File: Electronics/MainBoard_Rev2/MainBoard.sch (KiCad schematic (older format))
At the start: 4 parts

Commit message: Rev 3.0 is now done!
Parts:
- added D6: LED_Dual_AACC, LED_SMD:LED_RGB_1210, symbol Device:LED_Dual_AACC
- added D7: LED, LED_SMD:LED_0603_1608Metric, symbol Device:LED
- added H1, H2: MountingHole, MountingHole:MountingHole_3.2mm_M3_DIN965, symbol Mechanical:MountingHole
- added H3: MountingHole, Symbol:KiCad-Logo_5mm_SolderMask, symbol Mechanical:MountingHole
- added H4: MountingHole, Symbol:OSHW-Logo_5.7x6mm_SilkScreen, symbol Mechanical:MountingHole
- added H5: MountingHole, MainBoard_Rev2:QR_Link, symbol Mechanical:MountingHole
- added H6: MountingHole, MainBoard_Rev2:DragonIcon, symbol Mechanical:MountingHole
- added J1: Conn_01x04_Female, Connector_PinSocket_2.54mm:PinSocket_1x04_P2.54mm_Vertical, symbol Connector:Conn_01x04_Female
- added R2, R3, R5, R6: 2.2k, Resistor_SMD:R_0603_1608Metric, symbol Device:R_Small
- added R4: 220, Resistor_SMD:R_0603_1608Metric, symbol Device:R_Small
- C1, C2: renamed from C?; footprint (none) -> Capacitor_SMD:C_0603_1608Metric
- J2: renamed from J?; footprint (none) -> Connector_Dsub:DSUB-9_Female_Horizontal_P2.77x2.84mm_EdgePinOffset4.94mm_Housed_MountingHolesOffset7.48mm; Digi-Key (none) -> AE10921-ND; MPN (none) -> A-DF 09 A/KG-T2S
- U1: renamed from U?; Digi-Key (none) -> 1904-1025-1-ND; MPN (none) -> ESP32-WROOM-32D (16MB)
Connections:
- net +3V3: now also D6.1 (A1), D6.2 (A2), D7.2 (A), J1.2 (Pin_2), R5.1, R6.1
- net GND: now also J1.1 (Pin_1)
- net AUDIO: now reaches U1.10 (IO25)
- net IR_OUT: now reaches U1.11 (IO26)
- net LED_1: now reaches U1.12 (IO27)
- net VBRT: now reaches U1.16 (IO13)
- net TRIGGER: now reaches U1.23 (IO15)
- net IR_IN: now reaches U1.24 (IO2)
- net IR_IN: now also J2.3
- net CHG_STAT: now reaches U1.26 (IO4)
- net SDA: now reaches U1.27 (IO16)
- net SDA: now also J2.8, J1.4 (Pin_4), R6.2
- net SCL: now reaches U1.28 (IO17)
- net SCL: now also J2.4, J1.3 (Pin_3), R5.2
- net CHG_R: now reaches U1.30 (IO18)
- net CHG_R: now also R2.2
- net CHG_G: now reaches U1.31 (IO19)
- net CHG_G: now also R3.2
- net CONN_IND: now reaches U1.33 (IO21)
- net CONN_IND: now also R4.2
- net V_SENSE: now reaches U1.9 (IO33)
- net LED_2: now reaches J2.7
- new net: D6.4 (K2), R2.1
- new net: D6.3 (K1), R3.1
- new net: D7.1 (K), R4.1
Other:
- moved on the sheet: J2

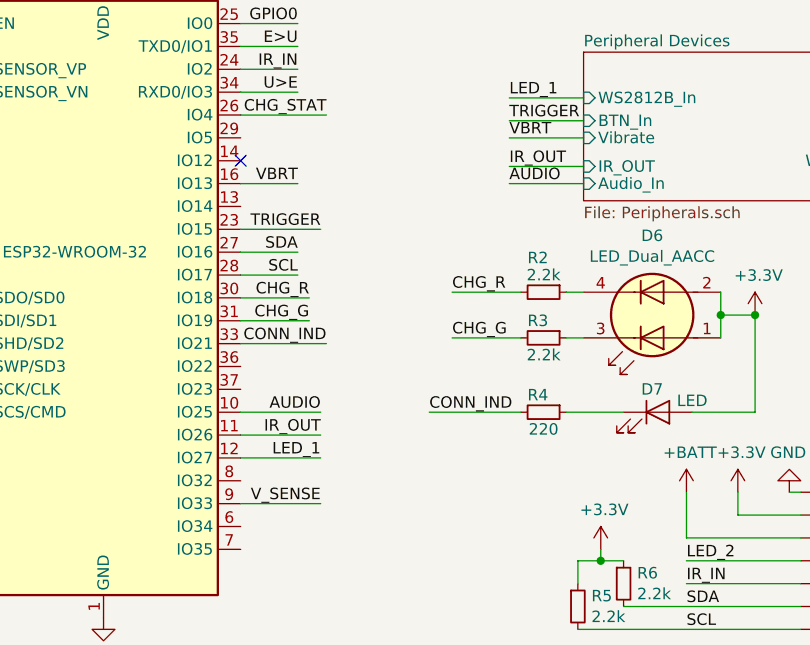
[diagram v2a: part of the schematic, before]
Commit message: Adjusted a few resistor values, added I2S pinout
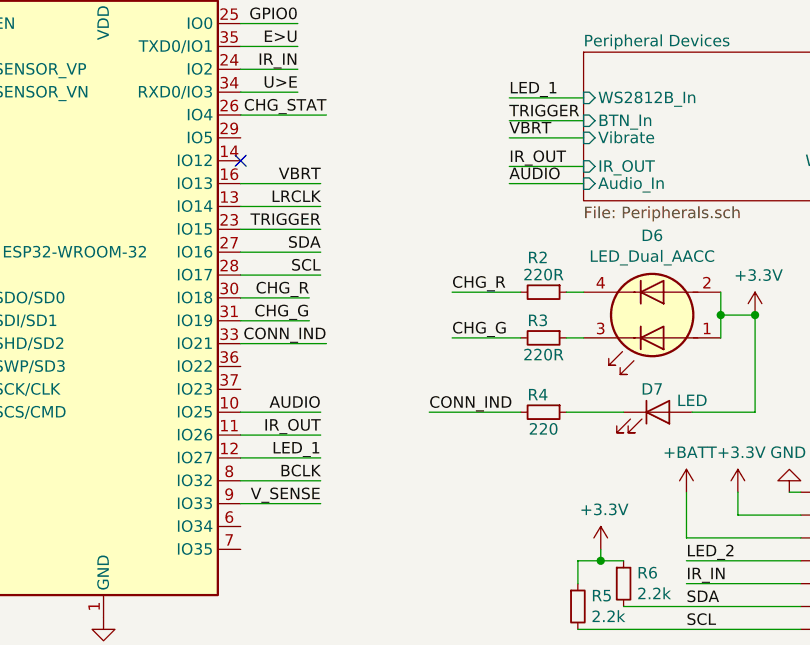
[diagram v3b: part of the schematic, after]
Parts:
- R2, R3: value 2.2k -> 220R
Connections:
- net LRCLK: now reaches U1.13 (IO14)
- net BCLK: now reaches U1.8 (IO32)
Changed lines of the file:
@@
 	6900 4400 6550 4400
 Wire Wire Line
-	6550 3000 6800 3000
-Text Label 6800 3000 2    50   ~ 0
+	6550 3000 6900 3000
+Text Label 6900 3000 2    50   ~ 0
 VBRT
 Text Label 7725 2800 0    50   ~ 0
@@
 P 7875 3475
 F 0 "R2" V 7725 3450 50  0000 C CNN
-F 1 "2.2k" V 7800 3475 50  0000 C CNN
+F 1 "220R" V 7800 3475 50  0000 C CNN
 F 2 "Resistor_SMD:R_0603_1608Metric" H 7875 3475 50  0001 C CNN
 F 3 "~" H 7875 3475 50  0001 C CNN
@@
 P 7875 3675
 F 0 "R3" V 7800 3650 50  0000 C CNN
-F 1 "2.2k" V 7950 3675 50  0000 C CNN
+F 1 "220R" V 7950 3675 50  0000 C CNN
 F 2 "Resistor_SMD:R_0603_1608Metric" H 7875 3675 50  0001 C CNN
 F 3 "~" H 7875 3675 50  0001 C CNN
@@
 IR_IN
 Wire Wire Line
-	6550 3300 6800 3300
-Wire Wire Line
-	6550 3400 6800 3400
-Text Label 6800 3300 2    50   ~ 0
+	6550 3300 6900 3300
+Wire Wire Line
+	6550 3400 6900 3400
+Text Label 6900 3300 2    50   ~ 0
 SDA
-Text Label 6800 3400 2    50   ~ 0
+Text Label 6900 3400 2    50   ~ 0
 SCL
 $Comp
@@
 Wire Wire Line
 	2600 3575 2600 4325
+Text Label 6900 4300 2    50   ~ 0
+BCLK
+Text Label 6900 3100 2    50   ~ 0
+LRCLK
+Wire Wire Line
+	6550 4300 6900 4300
+Wire Wire Line
+	6550 3100 6900 3100
 $EndSCHEMATC

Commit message: Began rework to even better hardware
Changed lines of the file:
@@
 Text Label 6800 2500 2    50   ~ 0
 IR_IN
-Wire Wire Line
-	6550 3300 6900 3300
-Wire Wire Line
-	6550 3400 6900 3400
 Text Label 6900 3300 2    50   ~ 0
 SDA
@@
 Wire Wire Line
 	6550 3100 6900 3100
+Text GLabel 6925 3300 2    50   Input ~ 0
+SDA
+Text GLabel 6925 3400 2    50   Input ~ 0
+SCL
+Wire Wire Line
+	6550 3400 6925 3400
+Wire Wire Line
+	6550 3300 6925 3300
 $EndSCHEMATC

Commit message: Temporary polishing of PCB
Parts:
- added AMP1: MAX98357A, Package_DFN_QFN:QFN-16-1EP_3x3mm_P0.5mm_EP2.7x2.7mm_ThermalVias, symbol XasParts:MAX98357A
- added C4: 10uF, Capacitor_SMD:C_0805_2012Metric, symbol Device:C_Small
- C1, C2: footprint Capacitor_SMD:C_0603_1608Metric -> Capacitor_SMD:C_0805_2012Metric
- R2, R3, R4, R5, R6: footprint Resistor_SMD:R_0603_1608Metric -> Resistor_SMD:R_0805_2012Metric
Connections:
- net +BATT: now also AMP1.4 (~MODE), AMP1.7 (Vdd), AMP1.8 (Vdd), C4.1
- net AUDIO: now also AMP1.1 (DIN)
- net BCLK: now also AMP1.16 (BCLK)
- net GND: now also AMP1.11 (GND), AMP1.15 (GND), AMP1.2 (GAIN), AMP1.3 (GND), C4.2
- net LRCLK: now also AMP1.14 (LRCLK)
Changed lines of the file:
@@
 F 0 "C1" V 6148 1600 50  0000 C CNN
 F 1 "10uF" V 6239 1600 50  0000 C CNN
-F 2 "Capacitor_SMD:C_0603_1608Metric" H 6438 1450 50  0001 C CNN
+F 2 "Capacitor_SMD:C_0805_2012Metric" H 6438 1450 50  0001 C CNN
 F 3 "~" H 6400 1600 50  0001 C CNN
 	1    6400 1600
@@
 F 0 "C2" V 6200 1900 50  0000 C CNN
 F 1 "150nF" V 6300 1800 50  0000 C CNN
-F 2 "Capacitor_SMD:C_0603_1608Metric" H 6400 1800 50  0001 C CNN
+F 2 "Capacitor_SMD:C_0805_2012Metric" H 6400 1800 50  0001 C CNN
 F 3 "~" H 6400 1800 50  0001 C CNN
 	1    6400 1800
@@
 F 0 "R2" V 7725 3450 50  0000 C CNN
 F 1 "220R" V 7800 3475 50  0000 C CNN
-F 2 "Resistor_SMD:R_0603_1608Metric" H 7875 3475 50  0001 C CNN
+F 2 "Resistor_SMD:R_0805_2012Metric" H 7875 3475 50  0001 C CNN
 F 3 "~" H 7875 3475 50  0001 C CNN
 	1    7875 3475
@@
 F 0 "R3" V 7800 3650 50  0000 C CNN
 F 1 "220R" V 7950 3675 50  0000 C CNN
-F 2 "Resistor_SMD:R_0603_1608Metric" H 7875 3675 50  0001 C CNN
+F 2 "Resistor_SMD:R_0805_2012Metric" H 7875 3675 50  0001 C CNN
 F 3 "~" H 7875 3675 50  0001 C CNN
 	1    7875 3675
@@
 F 0 "R4" V 7800 3975 50  0000 C CNN
 F 1 "220" V 7950 4000 50  0000 C CNN
-F 2 "Resistor_SMD:R_0603_1608Metric" H 7875 4000 50  0001 C CNN
+F 2 "Resistor_SMD:R_0805_2012Metric" H 7875 4000 50  0001 C CNN
 F 3 "~" H 7875 4000 50  0001 C CNN
 	1    7875 4000
@@
 F 0 "R6" H 8284 4796 50  0000 L CNN
 F 1 "2.2k" H 8284 4705 50  0000 L CNN
-F 2 "Resistor_SMD:R_0603_1608Metric" H 8225 4750 50  0001 C CNN
+F 2 "Resistor_SMD:R_0805_2012Metric" H 8225 4750 50  0001 C CNN
 F 3 "~" H 8225 4750 50  0001 C CNN
 	1    8225 4750
@@
 F 0 "R5" H 8084 4896 50  0000 L CNN
 F 1 "2.2k" H 8084 4805 50  0000 L CNN
-F 2 "Resistor_SMD:R_0603_1608Metric" H 8025 4850 50  0001 C CNN
+F 2 "Resistor_SMD:R_0805_2012Metric" H 8025 4850 50  0001 C CNN
 F 3 "~" H 8025 4850 50  0001 C CNN
 	1    8025 4850
@@
 Wire Wire Line
 	6550 3300 6925 3300
+$Comp
+L XasParts:MAX98357A AMP1
+U 1 1 5D27DFC9
+P 3925 6250
+F 0 "AMP1" H 4375 6250 50  0000 L CNN
+F 1 "MAX98357A" H 4350 6150 50  0000 L CNN
+F 2 "Package_DFN_QFN:QFN-16-1EP_3x3mm_P0.5mm_EP2.7x2.7mm_ThermalVias" H 4025 5900 50  0001 C CNN
+F 3 "" H 4025 5900 50  0001 C CNN
+	1    3925 6250
+	1    0    0    -1
+$EndComp
+Wire Wire Line
+	3875 5200 3925 5200
+Wire Wire Line
+	3925 5200 3925 5075
+Connection ~ 3925 5200
+Wire Wire Line
+	3925 5200 3975 5200
+$Comp
+L power:+BATT #PWR0117
+U 1 1 5D282552
+P 3925 5075
+F 0 "#PWR0117" H 3925 4925 50  0001 C CNN
+F 1 "+BATT" H 3940 5248 50  0000 C CNN
+F 2 "" H 3925 5075 50  0001 C CNN
+F 3 "" H 3925 5075 50  0001 C CNN
+	1    3925 5075
+	1    0    0    -1
+$EndComp
+$Comp
+L power:GND #PWR0118
+U 1 1 5D282625
+P 4025 6725
+F 0 "#PWR0118" H 4025 6475 50  0001 C CNN
+F 1 "GND" H 4030 6552 50  0000 C CNN
+F 2 "" H 4025 6725 50  0001 C CNN
+F 3 "" H 4025 6725 50  0001 C CNN
+	1    4025 6725
+	1    0    0    -1
+$EndComp
+Wire Wire Line
+	3925 6600 4025 6600
+Connection ~ 4025 6600
+Wire Wire Line
+	4025 6600 4125 6600
+Wire Wire Line
+	4025 6600 4025 6725
+Wire Wire Line
+	3525 5950 3200 5950
+Text Label 3200 5950 0    50   ~ 0
+LRCLK
+Text Label 3200 6050 0    50   ~ 0
+BCLK
+Wire Wire Line
+	3200 6050 3525 6050
+Wire Wire Line
+	3525 6150 3200 6150
+Text Label 3200 6150 0    50   ~ 0
+AUDIO
+Wire Wire Line
+	3525 5700 3525 5200
+Wire Wire Line
+	3525 5200 3875 5200
+Connection ~ 3875 5200
+$Comp
+L power:GND #PWR0119
+U 1 1 5D29AF62
+P 3200 5800
+F 0 "#PWR0119" H 3200 5550 50  0001 C CNN
+F 1 "GND" V 3205 5672 50  0000 R CNN
+F 2 "" H 3200 5800 50  0001 C CNN
+F 3 "" H 3200 5800 50  0001 C CNN
+	1    3200 5800
+	0    1    1    0
+$EndComp
+Wire Wire Line
+	3200 5800 3525 5800
+$Comp
+L Device:C_Small C4
+U 1 1 5D29F5C5
+P 3425 5200
+F 0 "C4" V 3196 5200 50  0000 C CNN
+F 1 "10uF" V 3287 5200 50  0000 C CNN
+F 2 "Capacitor_SMD:C_0805_2012Metric" H 3425 5200 50  0001 C CNN
+F 3 "~" H 3425 5200 50  0001 C CNN
+	1    3425 5200
+	0    1    1    0
+$EndComp
+Connection ~ 3525 5200
+$Comp
+L power:GND #PWR0120
+U 1 1 5D29F80C
+P 3325 5200
+F 0 "#PWR0120" H 3325 4950 50  0001 C CNN
+F 1 "GND" V 3330 5072 50  0000 R CNN
+F 2 "" H 3325 5200 50  0001 C CNN
+F 3 "" H 3325 5200 50  0001 C CNN
+	1    3325 5200
+	0    1    1    0
+$EndComp
 $EndSCHEMATC

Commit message: Began reworking the PCB
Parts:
- added C?: 47uF, Capacitor_SMD:C_1206_3216Metric, symbol Device:C
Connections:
- net +3V3: now also C?.2
- net GND: now also C?.1
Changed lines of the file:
@@
 	0    1    1    0
 $EndComp
+$Comp
+L Device:C C?
+U 1 1 5D67DBF1
+P 6400 1150
+F 0 "C?" V 6148 1150 50  0000 C CNN
+F 1 "47uF" V 6239 1150 50  0000 C CNN
+F 2 "Capacitor_SMD:C_1206_3216Metric" H 6438 1000 50  0001 C CNN
+F 3 "~" H 6400 1150 50  0001 C CNN
+	1    6400 1150
+	0    1    1    0
+$EndComp
+Wire Wire Line
+	6250 1150 6250 1600
+Connection ~ 6250 1600
+Wire Wire Line
+	6550 1150 6550 1600
+Connection ~ 6550 1600
 $EndSCHEMATC

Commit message: Began reworking sections
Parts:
- removed C1: 10uF, Capacitor_SMD:C_0805_2012Metric, symbol Device:C
- added R1, R7: 220, Resistor_SMD:R_0805_2012Metric, symbol Device:R_Small
- added TP1, TP2, TP3: TestPoint, TestPoint:TestPoint_Pad_2.0x2.0mm, symbol Connector:TestPoint
- AMP1: symbol XasParts:MAX98357A -> MainBoard-rescue:MAX98357A-XasParts
- gave numbers to parts that had none: 1
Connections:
- net +BATT: no longer AMP1.7 (Vdd)
- net AUDIO: now also TP3.1
- net BCLK: now also TP2.1
- net IR_IN: now also R7.2; no longer J2.3
- net LED_2: now also R1.2; no longer J2.7
- net LRCLK: now also TP1.1
- net CTRL_BACK: now reaches U1.29 (IO5)
- net CTRL_FWD: now reaches U1.36 (IO22)
- net CTRL_DOWN: now reaches U1.37 (IO23)
- new net: J2.3, R7.1
- new net: J2.7, R1.1
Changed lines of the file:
@@
 	5950 1750 5950 1800
-$Comp
-L Device:C C1
-U 1 1 5C2D5556
-P 6400 1600
-F 0 "C1" V 6148 1600 50  0000 C CNN
-F 1 "10uF" V 6239 1600 50  0000 C CNN
-F 2 "Capacitor_SMD:C_0805_2012Metric" H 6438 1450 50  0001 C CNN
-F 3 "~" H 6400 1600 50  0001 C CNN
-	1    6400 1600
-	0    1    1    0
-$EndComp
 $Comp
 L Device:C_Small C2
@@
 $EndComp
 Wire Wire Line
-	6250 1600 6250 1800
-Wire Wire Line
 	6250 1800 5950 1800
 Connection ~ 5950 1800
@@
 Wire Wire Line
 	6725 1800 6725 1875
-Wire Wire Line
-	6550 1600 6550 1800
 Connection ~ 6550 1800
 Wire Wire Line
@@
 F6 "IR_OUT" I L 8050 2925 50
 F7 "Audio_In" I L 8050 3000 50
+F8 "BACK" I R 9575 2550 50
+F9 "FWD" I R 9575 2625 50
+F10 "DOWN" I R 9575 2700 50
 $EndSheet
 Wire Wire Line
@@
 Wire Wire Line
 	9575 2900 9850 2900
-Wire Wire Line
-	9000 4650 8500 4650
 Text Label 8500 4650 0    50   ~ 0
 LED_2
@@
 	1    0    0    -1
 $EndComp
-Wire Wire Line
-	9000 4750 8500 4750
 Text Label 8500 4750 0    50   ~ 0
 IR_IN
@@
 	6550 3300 6925 3300
 $Comp
-L XasParts:MAX98357A AMP1
+L MainBoard-rescue:MAX98357A-XasParts AMP1
 U 1 1 5D27DFC9
 P 3925 6250
@@
 	1    0    0    -1
 $EndComp
-Wire Wire Line
-	3875 5200 3925 5200
 Wire Wire Line
 	3925 5200 3925 5075
@@
 Wire Wire Line
 	3525 5700 3525 5200
-Wire Wire Line
-	3525 5200 3875 5200
-Connection ~ 3875 5200
 $Comp
 L power:GND #PWR0119
@@
 $EndComp
 $Comp
-L Device:C C?
+L Device:C C5
 U 1 1 5D67DBF1
 P 6400 1150
-F 0 "C?" V 6148 1150 50  0000 C CNN
+F 0 "C5" V 6148 1150 50  0000 C CNN
 F 1 "47uF" V 6239 1150 50  0000 C CNN
 F 2 "Capacitor_SMD:C_1206_3216Metric" H 6438 1000 50  0001 C CNN
@@
 $EndComp
 Wire Wire Line
-	6250 1150 6250 1600
-Connection ~ 6250 1600
-Wire Wire Line
-	6550 1150 6550 1600
-Connection ~ 6550 1600
+	3525 5200 3925 5200
+$Comp
+L Device:R_Small R1
+U 1 1 5D6959C1
+P 8875 4650
+F 0 "R1" V 8900 4725 50  0000 C CNN
+F 1 "220" V 8900 4575 50  0000 C CNN
+F 2 "Resistor_SMD:R_0805_2012Metric" H 8875 4650 50  0001 C CNN
+F 3 "~" H 8875 4650 50  0001 C CNN
+	1    8875 4650
+	0    1    1    0
+$EndComp
+$Comp
+L Device:R_Small R7
+U 1 1 5D695A6F
+P 8875 4750
+F 0 "R7" V 8925 4825 50  0000 C CNN
+F 1 "220" V 8925 4675 50  0000 C CNN
+F 2 "Resistor_SMD:R_0805_2012Metric" H 8875 4750 50  0001 C CNN
+F 3 "~" H 8875 4750 50  0001 C CNN
+	1    8875 4750
+	0    1    1    0
+$EndComp
+Wire Wire Line
+	8975 4750 9000 4750
+Wire Wire Line
+	8975 4650 9000 4650
+Wire Wire Line
+	8500 4650 8775 4650
+Wire Wire Line
+	8500 4750 8775 4750
+Wire Wire Line
+	6550 2800 7025 2800
+Wire Wire Line
+	6550 3800 7025 3800
+Wire Wire Line
+	6550 3900 7025 3900
+Text Label 7025 2800 2    50   ~ 0
+CTRL_BACK
+Text Label 7025 3800 2    50   ~ 0
+CTRL_FWD
+Text Label 7025 3900 2    50   ~ 0
+CTRL_DOWN
+Wire Wire Line
+	9575 2550 10175 2550
+Text Label 10175 2550 2    50   ~ 0
+CTRL_BACK
+Text Label 10175 2625 2    50   ~ 0
+CTRL_FWD
+Text Label 10175 2700 2    50   ~ 0
+CTRL_DOWN
+Wire Wire Line
+	10175 2700 9575 2700
+Wire Wire Line
+	10175 2625 9575 2625
+$Comp
+L Connector:TestPoint TP1
+U 1 1 5D6C79CC
+P 3200 5950
+F 0 "TP1" V 3175 6550 50  0000 C CNN
+F 1 "TestPoint" V 3175 6300 50  0000 C CNN
+F 2 "TestPoint:TestPoint_Pad_2.0x2.0mm" H 3400 5950 50  0001 C CNN
+F 3 "~" H 3400 5950 50  0001 C CNN
+	1    3200 5950
+	0    -1   -1   0
+$EndComp
+$Comp
+L Connector:TestPoint TP2
+U 1 1 5D6C7B05
+P 3200 6050
+F 0 "TP2" V 3175 6650 50  0000 C CNN
+F 1 "TestPoint" V 3175 6400 50  0000 C CNN
+F 2 "TestPoint:TestPoint_Pad_2.0x2.0mm" H 3400 6050 50  0001 C CNN
+F 3 "~" H 3400 6050 50  0001 C CNN
+	1    3200 6050
+	0    -1   -1   0
+$EndComp
+$Comp
+L Connector:TestPoint TP3
+U 1 1 5D6C7BE2
+P 3200 6150
+F 0 "TP3" V 3175 6750 50  0000 C CNN
+F 1 "TestPoint" V 3175 6500 50  0000 C CNN
+F 2 "TestPoint:TestPoint_Pad_2.0x2.0mm" H 3400 6150 50  0001 C CNN
+F 3 "~" H 3400 6150 50  0001 C CNN
+	1    3200 6150
+	0    -1   -1   0
+$EndComp
+Wire Wire Line
+	6550 1150 6550 1800
+Wire Wire Line
+	6250 1150 6250 1800
 $EndSCHEMATC

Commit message: Continued work on the current electronics
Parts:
- removed H5: MountingHole, MainBoard_Rev2:QR_Link, symbol Mechanical:MountingHole
- added J5: Conn_01x02_Male, Connector_PinHeader_2.00mm:PinHeader_1x02_P2.00mm_Vertical, symbol Connector:Conn_01x02_Male
- added R8, R9: 220, Resistor_SMD:R_0805_2012Metric, symbol Device:R_Small
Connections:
- net SCL: now also R9.2; no longer J2.4
- net SDA: now also R8.2; no longer J2.8
- net at AMP1.10 (OUT-): now also J5.1 (Pin_1)
- net at AMP1.9 (OUT+): now also J5.2 (Pin_2)
- new net: J2.4, R9.1
- new net: J2.8, R8.1
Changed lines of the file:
@@
 $EndComp
-Wire Wire Line
-	8225 4850 9000 4850
-Wire Wire Line
-	8025 4950 9000 4950
 Wire Wire Line
 	8025 4750 8025 4650
@@
 	1    0    0    -1
 $EndComp
-$Comp
-L Mechanical:MountingHole H5
-U 1 1 5C311B5D
-P 1600 6650
-F 0 "H5" H 1700 6696 50  0000 L CNN
-F 1 "MountingHole" H 1700 6605 50  0000 L CNN
-F 2 "MainBoard_Rev2:QR_Link" H 1600 6650 50  0001 C CNN
-F 3 "~" H 1600 6650 50  0001 C CNN
-	1    1600 6650
-	1    0    0    -1
-$EndComp
 Wire Wire Line
 	6550 3700 6925 3700
@@
 Wire Wire Line
 	6250 1150 6250 1800
+$Comp
+L Connector:Conn_01x02_Male J5
+U 1 1 5D694850
+P 4925 5900
+F 0 "J5" H 4898 5780 50  0000 R CNN
+F 1 "Conn_01x02_Male" H 4898 5871 50  0000 R CNN
+F 2 "Connector_PinHeader_2.00mm:PinHeader_1x02_P2.00mm_Vertical" H 4925 5900 50  0001 C CNN
+F 3 "~" H 4925 5900 50  0001 C CNN
+	1    4925 5900
+	-1   0    0    1
+$EndComp
+Wire Wire Line
+	4475 5800 4725 5800
+Wire Wire Line
+	4475 5900 4725 5900
+$Comp
+L Device:R_Small R8
+U 1 1 5D69D2A7
+P 8875 4850
+F 0 "R8" V 8925 4925 50  0000 C CNN
+F 1 "220" V 8925 4775 50  0000 C CNN
+F 2 "Resistor_SMD:R_0805_2012Metric" H 8875 4850 50  0001 C CNN
+F 3 "~" H 8875 4850 50  0001 C CNN
+	1    8875 4850
+	0    1    1    0
+$EndComp
+$Comp
+L Device:R_Small R9
+U 1 1 5D69D35B
+P 8875 4950
+F 0 "R9" V 8925 5025 50  0000 C CNN
+F 1 "220" V 8925 4875 50  0000 C CNN
+F 2 "Resistor_SMD:R_0805_2012Metric" H 8875 4950 50  0001 C CNN
+F 3 "~" H 8875 4950 50  0001 C CNN
+	1    8875 4950
+	0    1    1    0
+$EndComp
+Wire Wire Line
+	8975 4850 9000 4850
+Wire Wire Line
+	8975 4950 9000 4950
+Wire Wire Line
+	8775 4850 8225 4850
+Wire Wire Line
+	8775 4950 8025 4950
 $EndSCHEMATC
